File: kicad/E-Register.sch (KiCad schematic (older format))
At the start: 19 parts, among them U113 74LS245, U114 74LS173, U115 74LS173

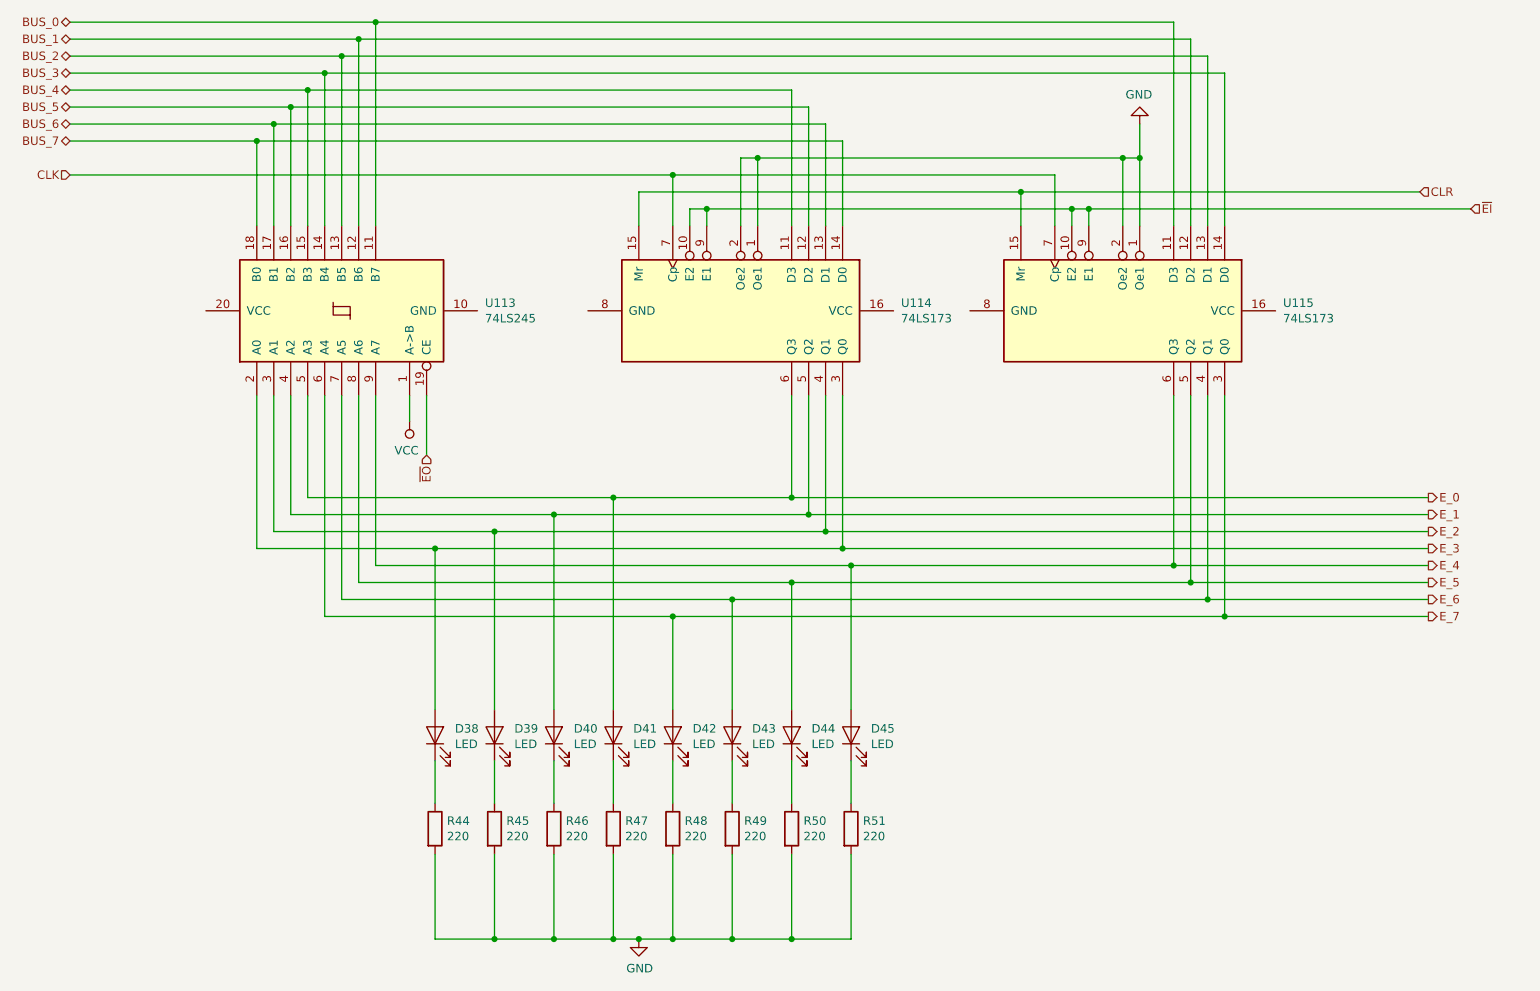
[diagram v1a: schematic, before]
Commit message: Reorganize part references
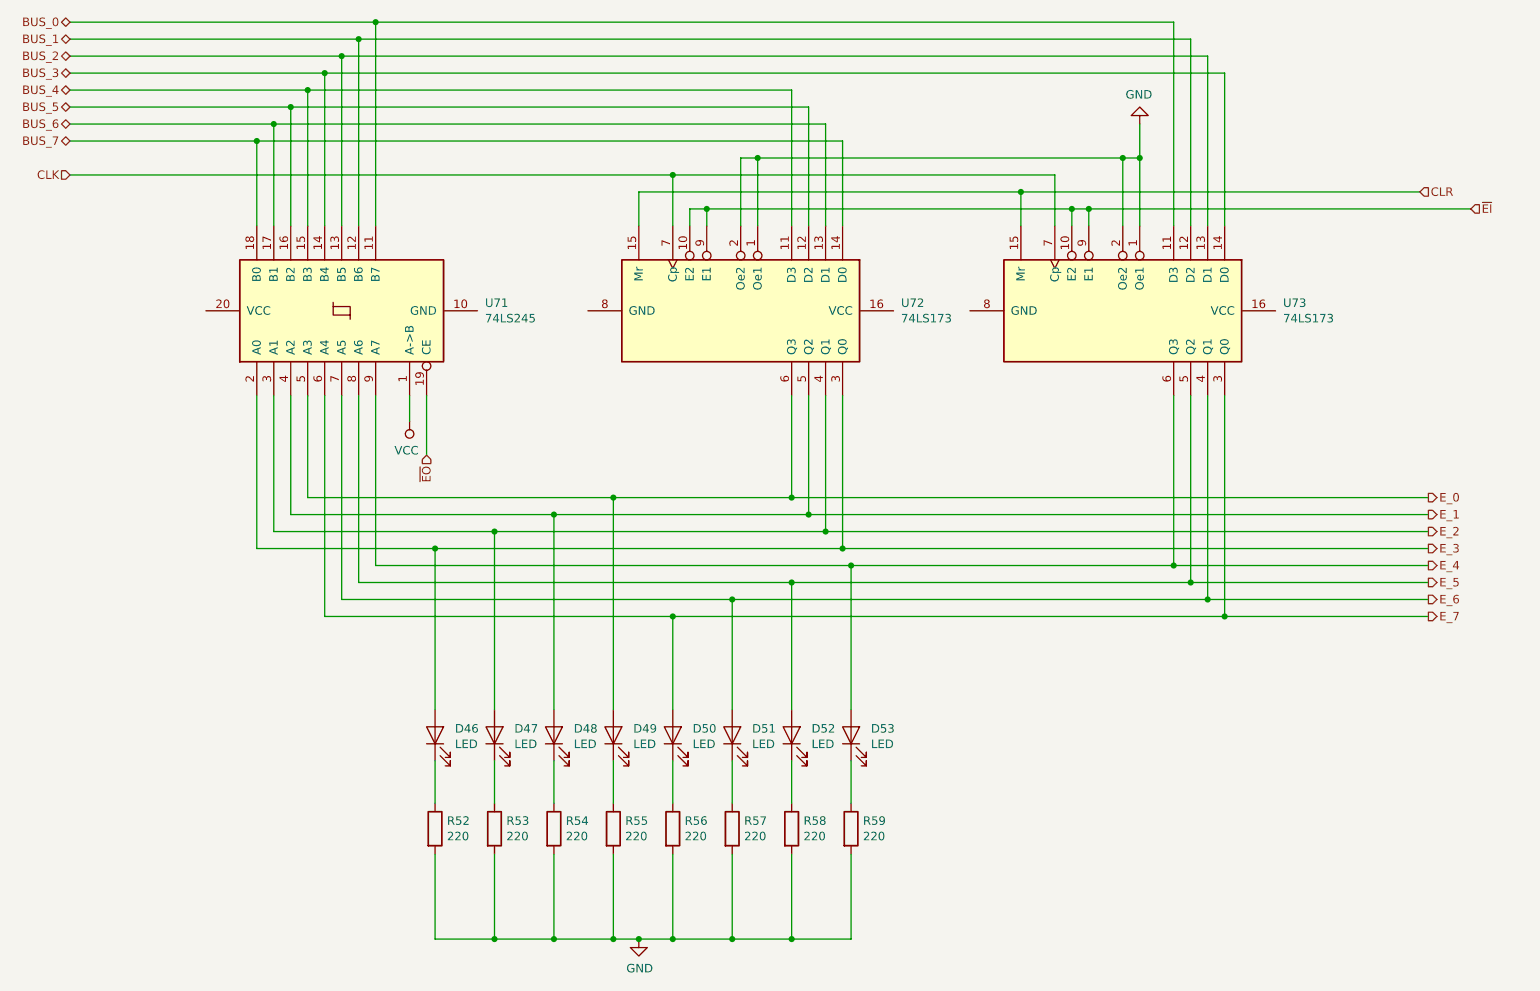
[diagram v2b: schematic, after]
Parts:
- renumbered D38 to D46, D39 to D47, D40 to D48, D41 to D49, D42 to D50, D43 to D51, D44 to D52, D45 to D53, R44 to R52, R45 to R53, R46 to R54, R47 to R55, R48 to R56, R49 to R57, R50 to R58, R51 to R59, U113 to U71, U114 to U72, U115 to U73
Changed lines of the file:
@@
 $Descr USLetter 11000 8500
 encoding utf-8
-Sheet 3 26
+Sheet 19 26
 Title "E Register"
 Date "2019-10-03"
@@
 AR Path="/5D9C73BD/5DA2C3AD" Ref="U?"  Part="1"
 AR Path="/5D9E8388/5DA2C3AD" Ref="U?"  Part="1"
-AR Path="/5DA98D6D/5DA9A55B/5DA2C3AD" Ref="U113"  Part="1"
-F 0 "U113" V 2946 2156 50  0000 R CNN
+AR Path="/5DA98D6D/5DA9A55B/5DA2C3AD" Ref="U71"  Part="1"
+F 0 "U71" V 2946 2156 50  0000 R CNN
 F 1 "74LS245" V 2855 2156 50  0000 R CNN
 F 2 "" H 2900 3000 50  0001 C CNN
@@
 AR Path="/5D9C73BD/5DA2C3DA" Ref="U?"  Part="1"
 AR Path="/5D9E8388/5DA2C3DA" Ref="U?"  Part="1"
-AR Path="/5DA98D6D/5DA9A55B/5DA2C3DA" Ref="U115"  Part="1"
-F 0 "U115" V 7454 3944 50  0000 L CNN
+AR Path="/5DA98D6D/5DA9A55B/5DA2C3DA" Ref="U73"  Part="1"
+F 0 "U73" V 7454 3944 50  0000 L CNN
 F 1 "74LS173" V 7545 3944 50  0000 L CNN
 F 2 "" H 7500 3000 50  0001 C CNN
@@
 AR Path="/5D9C73BD/5DA2C404" Ref="D?"  Part="1"
 AR Path="/5D9E8388/5DA2C404" Ref="D?"  Part="1"
-AR Path="/5DA98D6D/5DA9A55B/5DA2C404" Ref="D38"  Part="1"
-F 0 "D38" V 3489 5383 50  0000 R CNN
+AR Path="/5DA98D6D/5DA9A55B/5DA2C404" Ref="D46"  Part="1"
+F 0 "D46" V 3489 5383 50  0000 R CNN
 F 1 "LED" V 3398 5383 50  0000 R CNN
 F 2 "" H 3450 5500 50  0001 C CNN
@@
 AR Path="/5D9C73BD/5DA2C40A" Ref="D?"  Part="1"
 AR Path="/5D9E8388/5DA2C40A" Ref="D?"  Part="1"
-AR Path="/5DA98D6D/5DA9A55B/5DA2C40A" Ref="D39"  Part="1"
-F 0 "D39" V 3839 5383 50  0000 R CNN
+AR Path="/5DA98D6D/5DA9A55B/5DA2C40A" Ref="D47"  Part="1"
+F 0 "D47" V 3839 5383 50  0000 R CNN
 F 1 "LED" V 3748 5383 50  0000 R CNN
 F 2 "" H 3800 5500 50  0001 C CNN
@@
 AR Path="/5D9C73BD/5DA2C410" Ref="D?"  Part="1"
 AR Path="/5D9E8388/5DA2C410" Ref="D?"  Part="1"
-AR Path="/5DA98D6D/5DA9A55B/5DA2C410" Ref="D40"  Part="1"
-F 0 "D40" V 4189 5383 50  0000 R CNN
+AR Path="/5DA98D6D/5DA9A55B/5DA2C410" Ref="D48"  Part="1"
+F 0 "D48" V 4189 5383 50  0000 R CNN
 F 1 "LED" V 4098 5383 50  0000 R CNN
 F 2 "" H 4150 5500 50  0001 C CNN
@@
 AR Path="/5D9C73BD/5DA2C416" Ref="D?"  Part="1"
 AR Path="/5D9E8388/5DA2C416" Ref="D?"  Part="1"
-AR Path="/5DA98D6D/5DA9A55B/5DA2C416" Ref="D41"  Part="1"
-F 0 "D41" V 4539 5383 50  0000 R CNN
+AR Path="/5DA98D6D/5DA9A55B/5DA2C416" Ref="D49"  Part="1"
+F 0 "D49" V 4539 5383 50  0000 R CNN
 F 1 "LED" V 4448 5383 50  0000 R CNN
 F 2 "" H 4500 5500 50  0001 C CNN
@@
 AR Path="/5D9C73BD/5DA2C41C" Ref="D?"  Part="1"
 AR Path="/5D9E8388/5DA2C41C" Ref="D?"  Part="1"
-AR Path="/5DA98D6D/5DA9A55B/5DA2C41C" Ref="D42"  Part="1"
-F 0 "D42" V 4889 5383 50  0000 R CNN
+AR Path="/5DA98D6D/5DA9A55B/5DA2C41C" Ref="D50"  Part="1"
+F 0 "D50" V 4889 5383 50  0000 R CNN
 F 1 "LED" V 4798 5383 50  0000 R CNN
 F 2 "" H 4850 5500 50  0001 C CNN
@@
 AR Path="/5D9C73BD/5DA2C422" Ref="D?"  Part="1"
 AR Path="/5D9E8388/5DA2C422" Ref="D?"  Part="1"
-AR Path="/5DA98D6D/5DA9A55B/5DA2C422" Ref="D43"  Part="1"
-F 0 "D43" V 5239 5383 50  0000 R CNN
+AR Path="/5DA98D6D/5DA9A55B/5DA2C422" Ref="D51"  Part="1"
+F 0 "D51" V 5239 5383 50  0000 R CNN
 F 1 "LED" V 5148 5383 50  0000 R CNN
 F 2 "" H 5200 5500 50  0001 C CNN
@@
 AR Path="/5D9C73BD/5DA2C428" Ref="D?"  Part="1"
 AR Path="/5D9E8388/5DA2C428" Ref="D?"  Part="1"
-AR Path="/5DA98D6D/5DA9A55B/5DA2C428" Ref="D44"  Part="1"
-F 0 "D44" V 5589 5383 50  0000 R CNN
+AR Path="/5DA98D6D/5DA9A55B/5DA2C428" Ref="D52"  Part="1"
+F 0 "D52" V 5589 5383 50  0000 R CNN
 F 1 "LED" V 5498 5383 50  0000 R CNN
 F 2 "" H 5550 5500 50  0001 C CNN
@@
 AR Path="/5D9C73BD/5DA2C42E" Ref="D?"  Part="1"
 AR Path="/5D9E8388/5DA2C42E" Ref="D?"  Part="1"
-AR Path="/5DA98D6D/5DA9A55B/5DA2C42E" Ref="D45"  Part="1"
-F 0 "D45" V 5939 5383 50  0000 R CNN
+AR Path="/5DA98D6D/5DA9A55B/5DA2C42E" Ref="D53"  Part="1"
+F 0 "D53" V 5939 5383 50  0000 R CNN
 F 1 "LED" V 5848 5383 50  0000 R CNN
 F 2 "" H 5900 5500 50  0001 C CNN
@@
 AR Path="/5D9C73BD/5DA2C44A" Ref="R?"  Part="1"
 AR Path="/5D9E8388/5DA2C44A" Ref="R?"  Part="1"
-AR Path="/5DA98D6D/5DA9A55B/5DA2C44A" Ref="R44"  Part="1"
-F 0 "R44" H 3520 6096 50  0000 L CNN
+AR Path="/5DA98D6D/5DA9A55B/5DA2C44A" Ref="R52"  Part="1"
+F 0 "R52" H 3520 6096 50  0000 L CNN
 F 1 "220" H 3520 6005 50  0000 L CNN
 F 2 "" V 3380 6050 50  0001 C CNN
@@
 AR Path="/5D9C73BD/5DA2C450" Ref="R?"  Part="1"
 AR Path="/5D9E8388/5DA2C450" Ref="R?"  Part="1"
-AR Path="/5DA98D6D/5DA9A55B/5DA2C450" Ref="R45"  Part="1"
-F 0 "R45" H 3870 6096 50  0000 L CNN
+AR Path="/5DA98D6D/5DA9A55B/5DA2C450" Ref="R53"  Part="1"
+F 0 "R53" H 3870 6096 50  0000 L CNN
 F 1 "220" H 3870 6005 50  0000 L CNN
 F 2 "" V 3730 6050 50  0001 C CNN
@@
 AR Path="/5D9C73BD/5DA2C456" Ref="R?"  Part="1"
 AR Path="/5D9E8388/5DA2C456" Ref="R?"  Part="1"
-AR Path="/5DA98D6D/5DA9A55B/5DA2C456" Ref="R46"  Part="1"
-F 0 "R46" H 4220 6096 50  0000 L CNN
+AR Path="/5DA98D6D/5DA9A55B/5DA2C456" Ref="R54"  Part="1"
+F 0 "R54" H 4220 6096 50  0000 L CNN
 F 1 "220" H 4220 6005 50  0000 L CNN
 F 2 "" V 4080 6050 50  0001 C CNN
@@
 AR Path="/5D9C73BD/5DA2C45C" Ref="R?"  Part="1"
 AR Path="/5D9E8388/5DA2C45C" Ref="R?"  Part="1"
-AR Path="/5DA98D6D/5DA9A55B/5DA2C45C" Ref="R47"  Part="1"
-F 0 "R47" H 4570 6096 50  0000 L CNN
+AR Path="/5DA98D6D/5DA9A55B/5DA2C45C" Ref="R55"  Part="1"
+F 0 "R55" H 4570 6096 50  0000 L CNN
 F 1 "220" H 4570 6005 50  0000 L CNN
 F 2 "" V 4430 6050 50  0001 C CNN
@@
 AR Path="/5D9C73BD/5DA2C462" Ref="R?"  Part="1"
 AR Path="/5D9E8388/5DA2C462" Ref="R?"  Part="1"
-AR Path="/5DA98D6D/5DA9A55B/5DA2C462" Ref="R48"  Part="1"
-F 0 "R48" H 4920 6096 50  0000 L CNN
+AR Path="/5DA98D6D/5DA9A55B/5DA2C462" Ref="R56"  Part="1"
+F 0 "R56" H 4920 6096 50  0000 L CNN
 F 1 "220" H 4920 6005 50  0000 L CNN
 F 2 "" V 4780 6050 50  0001 C CNN
@@
 AR Path="/5D9C73BD/5DA2C468" Ref="R?"  Part="1"
 AR Path="/5D9E8388/5DA2C468" Ref="R?"  Part="1"
-AR Path="/5DA98D6D/5DA9A55B/5DA2C468" Ref="R49"  Part="1"
-F 0 "R49" H 5270 6096 50  0000 L CNN
+AR Path="/5DA98D6D/5DA9A55B/5DA2C468" Ref="R57"  Part="1"
+F 0 "R57" H 5270 6096 50  0000 L CNN
 F 1 "220" H 5270 6005 50  0000 L CNN
 F 2 "" V 5130 6050 50  0001 C CNN
@@
 AR Path="/5D9C73BD/5DA2C46E" Ref="R?"  Part="1"
 AR Path="/5D9E8388/5DA2C46E" Ref="R?"  Part="1"
-AR Path="/5DA98D6D/5DA9A55B/5DA2C46E" Ref="R50"  Part="1"
-F 0 "R50" H 5620 6096 50  0000 L CNN
+AR Path="/5DA98D6D/5DA9A55B/5DA2C46E" Ref="R58"  Part="1"
+F 0 "R58" H 5620 6096 50  0000 L CNN
 F 1 "220" H 5620 6005 50  0000 L CNN
 F 2 "" V 5480 6050 50  0001 C CNN
@@
 AR Path="/5D9C73BD/5DA2C474" Ref="R?"  Part="1"
 AR Path="/5D9E8388/5DA2C474" Ref="R?"  Part="1"
-AR Path="/5DA98D6D/5DA9A55B/5DA2C474" Ref="R51"  Part="1"
-F 0 "R51" H 5970 6096 50  0000 L CNN
+AR Path="/5DA98D6D/5DA9A55B/5DA2C474" Ref="R59"  Part="1"
+F 0 "R59" H 5970 6096 50  0000 L CNN
 F 1 "220" H 5970 6005 50  0000 L CNN
 F 2 "" V 5830 6050 50  0001 C CNN
@@
 AR Path="/5D9C73BD/5DA2C4C5" Ref="U?"  Part="1"
 AR Path="/5D9E8388/5DA2C4C5" Ref="U?"  Part="1"
-AR Path="/5DA98D6D/5DA9A55B/5DA2C4C5" Ref="U114"  Part="1"
-F 0 "U114" V 5204 3944 50  0000 L CNN
+AR Path="/5DA98D6D/5DA9A55B/5DA2C4C5" Ref="U72"  Part="1"
+F 0 "U72" V 5204 3944 50  0000 L CNN
 F 1 "74LS173" V 5295 3944 50  0000 L CNN
 F 2 "" H 5250 3000 50  0001 C CNN
